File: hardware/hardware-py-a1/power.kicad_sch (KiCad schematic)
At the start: 24 parts, among them Q1 AO3401A, Q2 BSS138, Q3 AO3401A, Q5 AO4953A, U1 LTC4054, U2 STI3411A, U5 XC6206PxxxMR

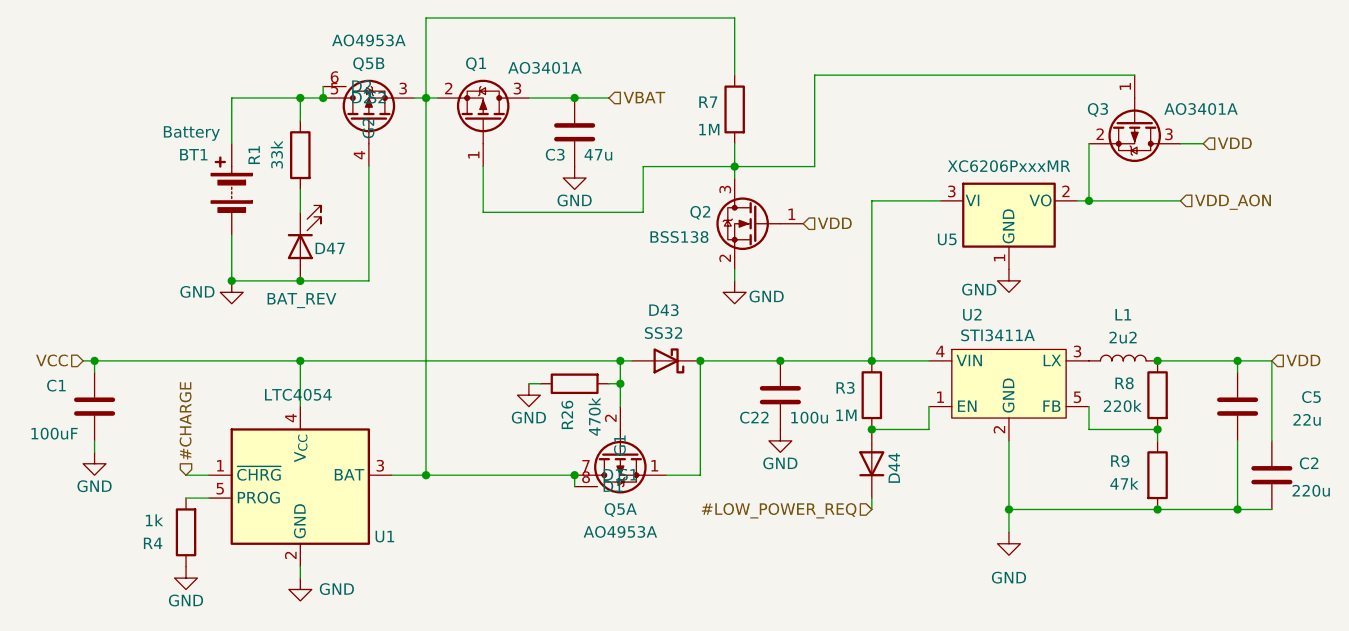
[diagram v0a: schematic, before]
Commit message: hw: passives values simpler, tantlum caps, silkscreen tweaks
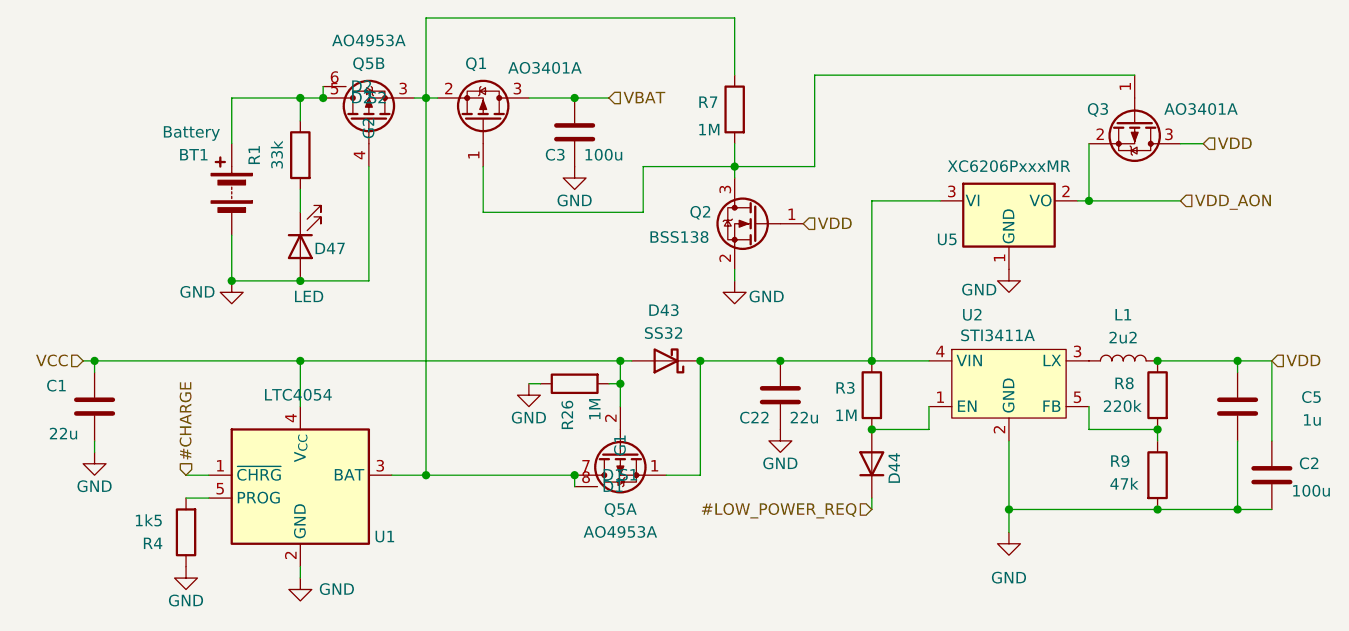
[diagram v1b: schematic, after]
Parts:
- C1: value 100uF -> 22u; footprint Capacitor_SMD:C_1210_3225Metric -> Capacitor_SMD:C_1206_3216Metric_Pad1.33x1.80mm_HandSolder
- C2: value 220u -> 100u; footprint Capacitor_SMD:C_2220_5750Metric -> Capacitor_Tantalum_SMD:CP_EIA-7343-31_Kemet-D
- C22: value 100u -> 22u; footprint Capacitor_SMD:C_1210_3225Metric_Pad1.33x2.70mm_HandSolder -> Capacitor_SMD:C_1206_3216Metric_Pad1.33x1.80mm_HandSolder
- C3: value 47u -> 100u; footprint Capacitor_SMD:C_1210_3225Metric_Pad1.33x2.70mm_HandSolder -> Capacitor_Tantalum_SMD:CP_EIA-7343-31_Kemet-D
- C5: value 22u -> 1u; footprint Capacitor_SMD:C_1210_3225Metric -> Capacitor_SMD:C_0805_2012Metric_Pad1.18x1.45mm_HandSolder
- D44: value D -> 1N4148
- D47: value BAT_REV -> LED
- R26: value 470k -> 1M
- R4: value 1k -> 1k5
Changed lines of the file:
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@@
 			)
 		)
-		(property "Value" "22u"
+		(property "Value" "1u"
 			(at 220.218 115.824 0)
 			(effects
@@
 			)
 		)
-		(property "Footprint" "Capacitor_SMD:C_1210_3225Metric"
+		(property "Footprint" "Capacitor_SMD:C_0805_2012Metric_Pad1.18x1.45mm_HandSolder"
 			(at 209.8548 118.11 0)
 			(effects
@@
 			)
 		)
-		(property "Value" "100uF"
+		(property "Value" "22u"
 			(at 82.042 117.348 0)
 			(effects
@@
 			)
 		)
-		(property "Footprint" "Capacitor_SMD:C_1210_3225Metric"
+		(property "Footprint" "Capacitor_SMD:C_1206_3216Metric_Pad1.33x1.80mm_HandSolder"
 			(at 82.8548 118.11 0)
 			(effects
@@
 			)
 		)
-		(property "Value" "220u"
+		(property "Value" "100u"
 			(at 221.234 123.698 0)
 			(effects
@@
 			)
 		)
-		(property "Footprint" "Capacitor_SMD:C_2220_5750Metric"
+		(property "Footprint" "Capacitor_Tantalum_SMD:CP_EIA-7343-31_Kemet-D"
 			(at 213.6648 125.73 0)
 			(effects
@@
 			)
 		)
-		(property "Value" "BAT_REV"
-			(at 102.87 102.362 90)
+		(property "Value" "LED"
+			(at 105.918 102.108 90)
 			(effects
 				(font
@@
 			)
 		)
-		(property "Value" "470k"
+		(property "Value" "1M"
 			(at 139.446 113.284 0)
 			(effects
@@
 			)
 		)
-		(property "Value" "100u"
+		(property "Value" "22u"
 			(at 161.036 115.57 0)
 			(effects
@@
 			)
 		)
-		(property "Footprint" "Capacitor_SMD:C_1210_3225Metric_Pad1.33x2.70mm_HandSolder"
+		(property "Footprint" "Capacitor_SMD:C_1206_3216Metric_Pad1.33x1.80mm_HandSolder"
 			(at 160.9852 116.84 0)
 			(effects
@@
 			)
 		)
-		(property "Value" "D"
+		(property "Value" "1N4148"
 			(at 172.72 121.92 90)
 			(effects
@@
 			)
 		)
-		(property "Value" "47u"
+		(property "Value" "100u"
 			(at 138.176 86.36 0)
 			(effects
@@
 			)
 		)
-		(property "Footprint" "Capacitor_SMD:C_1210_3225Metric_Pad1.33x2.70mm_HandSolder"
+		(property "Footprint" "Capacitor_Tantalum_SMD:CP_EIA-7343-31_Kemet-D"
 			(at 138.1252 87.63 0)
 			(effects
@@
 			)
 		)
-		(property "Value" "1k"
+		(property "Value" "1k5"
 			(at 91.44 127 0)
 			(effects
